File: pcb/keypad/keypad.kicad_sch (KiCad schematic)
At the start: 0 parts

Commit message: Keypad Layout Done V1
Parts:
- added BT1: Battery_Cell, Connector_JST:JST_PH_S2B-PH-SM4-TB_1x02-1MP_P2.00mm_Horizontal, symbol Device:Battery_Cell
- added J1: Conn_01x24_Male, Connector_FFC-FPC:TE_2-1734839-4_1x24-1MP_P0.5mm_Horizontal, symbol Connector:Conn_01x24_Male
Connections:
- net Keys/KC0: now also J1.16 (Pin_16)
- net Keys/KC1: now also J1.15 (Pin_15)
- net Keys/KC2: now also J1.14 (Pin_14)
- net Keys/KC3: now also J1.13 (Pin_13)
- net Keys/KC4: now also J1.12 (Pin_12)
- net Keys/KC5: now also J1.11 (Pin_11)
- net Keys/KC6: now also J1.10 (Pin_10)
- net Keys/KR0: now also J1.23 (Pin_23)
- net Keys/KR1: now also J1.22 (Pin_22)
- net Keys/KR2: now also J1.21 (Pin_21)
- net Keys/KR3: now also J1.20 (Pin_20)
- net Keys/KR4: now also J1.19 (Pin_19)
- net Keys/KR5: now also J1.18 (Pin_18)
- net Keys/KR6: now also J1.17 (Pin_17)
- net Keys/ON: now also J1.9 (Pin_9)
- new net GND: BT1.2 (-), J1.24 (Pin_24), J1.6 (Pin_6), J1.7 (Pin_7), J1.8 (Pin_8)
- new net VBAT: BT1.1 (+), J1.2 (Pin_2), J1.3 (Pin_3), J1.4 (Pin_4), J1.5 (Pin_5)
- no-connect marks 0 -> 1

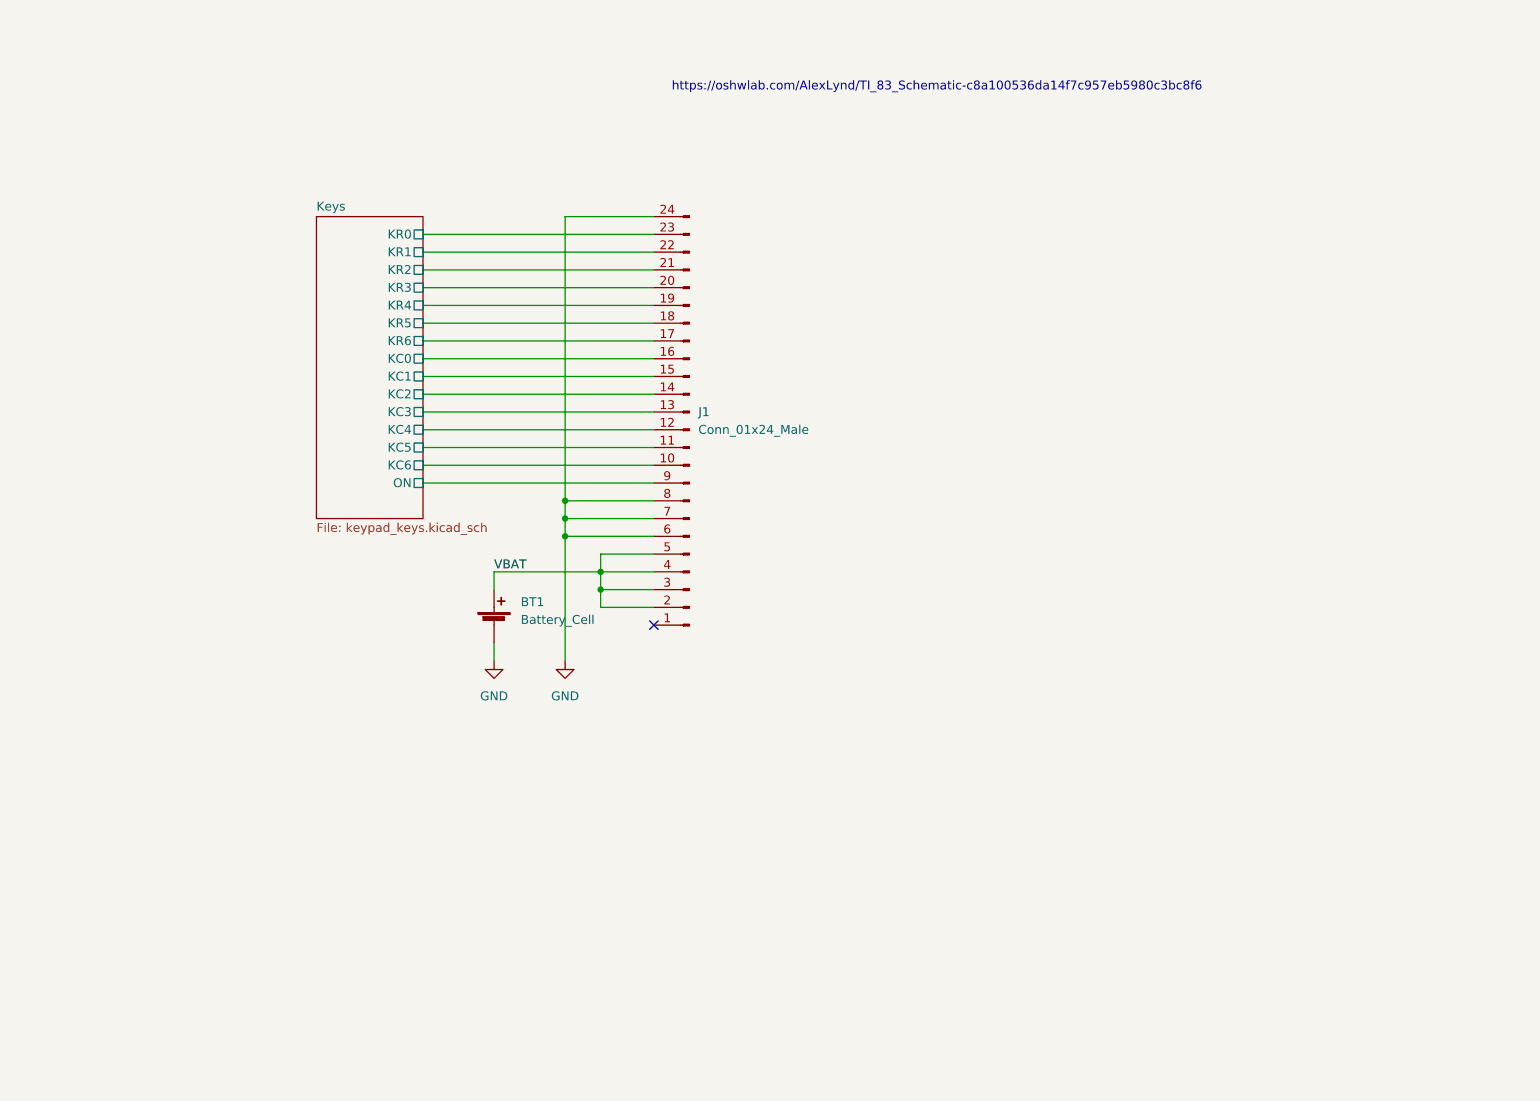
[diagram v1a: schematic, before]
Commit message: Keypad Schematic Update - Comm Interface
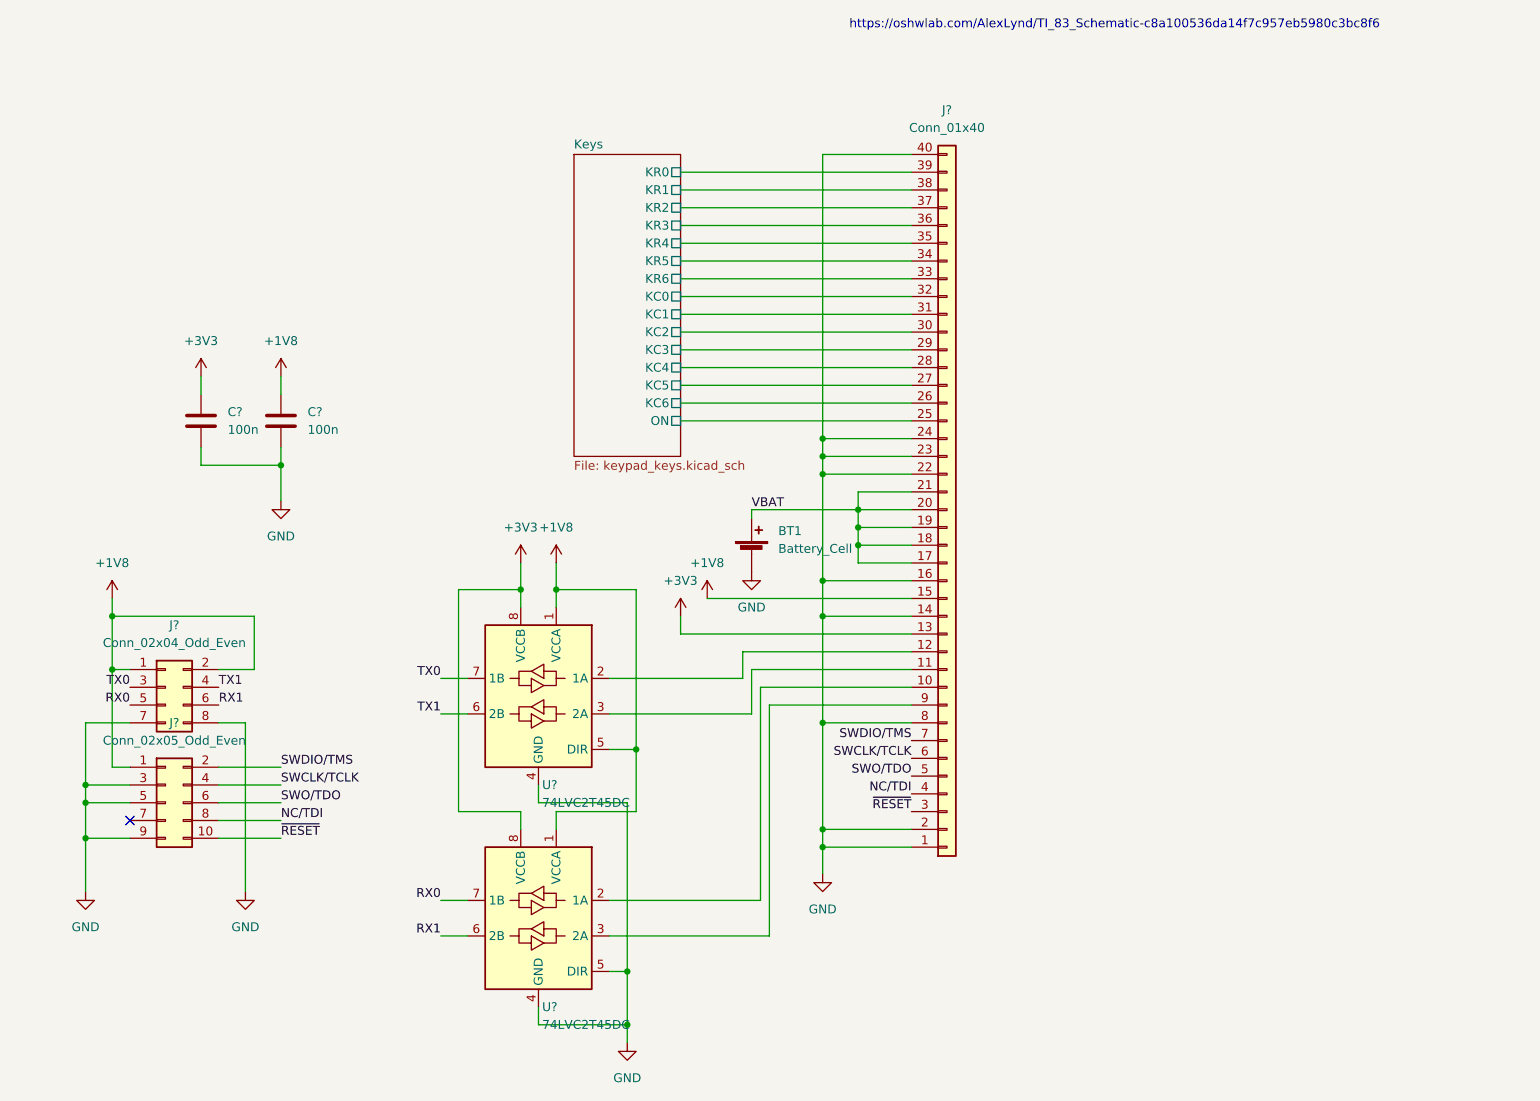
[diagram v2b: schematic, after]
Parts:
- removed J1: Conn_01x24_Male, Connector_FFC-FPC:TE_2-1734839-4_1x24-1MP_P0.5mm_Horizontal, symbol Connector:Conn_01x24_Male
- added C? (x2): 100n, Capacitor_SMD:C_0805_2012Metric, symbol Device:C
- added J?: Conn_01x40, Connector_FFC-FPC:TE_4-1734839-0_1x40-1MP_P0.5mm_Horizontal, symbol Connector_Generic:Conn_01x40
- added J?: Conn_02x04_Odd_Even, Connector_PinHeader_1.27mm:PinHeader_2x04_P1.27mm_Vertical_SMD, symbol Connector_Generic:Conn_02x04_Odd_Even
- added J?: Conn_02x05_Odd_Even, Connector_PinHeader_1.27mm:PinHeader_2x05_P1.27mm_Vertical_SMD, symbol Connector_Generic:Conn_02x05_Odd_Even
- added U? (x2): 74LVC2T45DC, Package_SO:VSSOP-8_2.3x2mm_P0.5mm, symbol Logic_LevelTranslator:74LVC2T45DC
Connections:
- net GND: now also C?.2, C?.2, J?.1 (Pin_1), J?.14 (Pin_14), J?.16 (Pin_16), J?.2 (Pin_2), J?.22 (Pin_22), J?.23 (Pin_23), J?.24 (Pin_24), J?.3 (Pin_3), J?.40 (Pin_40), J?.5 (Pin_5), J?.7 (Pin_7), J?.8 (Pin_8), J?.8 (Pin_8), J?.9 (Pin_9), U?.4 (GND), U?.4 (GND), U?.5 (DIR)
- net Keys/KC0: now also J?.32 (Pin_32)
- net Keys/KC1: now also J?.31 (Pin_31)
- net Keys/KC2: now also J?.30 (Pin_30)
- net Keys/KC3: now also J?.29 (Pin_29)
- net Keys/KC4: now also J?.28 (Pin_28)
- net Keys/KC5: now also J?.27 (Pin_27)
- net Keys/KC6: now also J?.26 (Pin_26)
- net Keys/KR0: now also J?.39 (Pin_39)
- net Keys/KR1: now also J?.38 (Pin_38)
- net Keys/KR2: now also J?.37 (Pin_37)
- net Keys/KR3: now also J?.36 (Pin_36)
- net Keys/KR4: now also J?.35 (Pin_35)
- net Keys/KR5: now also J?.34 (Pin_34)
- net Keys/KR6: now also J?.33 (Pin_33)
- net Keys/ON: now also J?.25 (Pin_25)
- net VBAT: now also J?.17 (Pin_17), J?.18 (Pin_18), J?.19 (Pin_19), J?.20 (Pin_20), J?.21 (Pin_21)
- new net: J?.10 (Pin_10), U?.2 (1A)
- new net: J?.11 (Pin_11), U?.3 (2A)
- new net: J?.12 (Pin_12), U?.2 (1A)
- new net: J?.9 (Pin_9), U?.3 (2A)
- new net +1V8: C?.1, J?.1 (Pin_1), J?.1 (Pin_1), J?.15 (Pin_15), J?.2 (Pin_2), U?.1 (VCCA), U?.1 (VCCA), U?.5 (DIR)
- new net +3V3: C?.1, J?.13 (Pin_13), U?.8 (VCCB), U?.8 (VCCB)
- new net NC/TDI: J?.4 (Pin_4), J?.8 (Pin_8)
- new net RX0: J?.5 (Pin_5), U?.7 (1B)
- new net RX1: J?.6 (Pin_6), U?.6 (2B)
- new net SWCLK/TCLK: J?.4 (Pin_4), J?.6 (Pin_6)
- new net SWDIO/TMS: J?.2 (Pin_2), J?.7 (Pin_7)
- new net SWO/TDO: J?.5 (Pin_5), J?.6 (Pin_6)
- new net TX0: J?.3 (Pin_3), U?.7 (1B)
- new net TX1: J?.4 (Pin_4), U?.6 (2B)
- new net ~{RESET}: J?.10 (Pin_10), J?.3 (Pin_3)
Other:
- moved on the sheet: BT1

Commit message: Keypad Layout Update - JTAG/UART
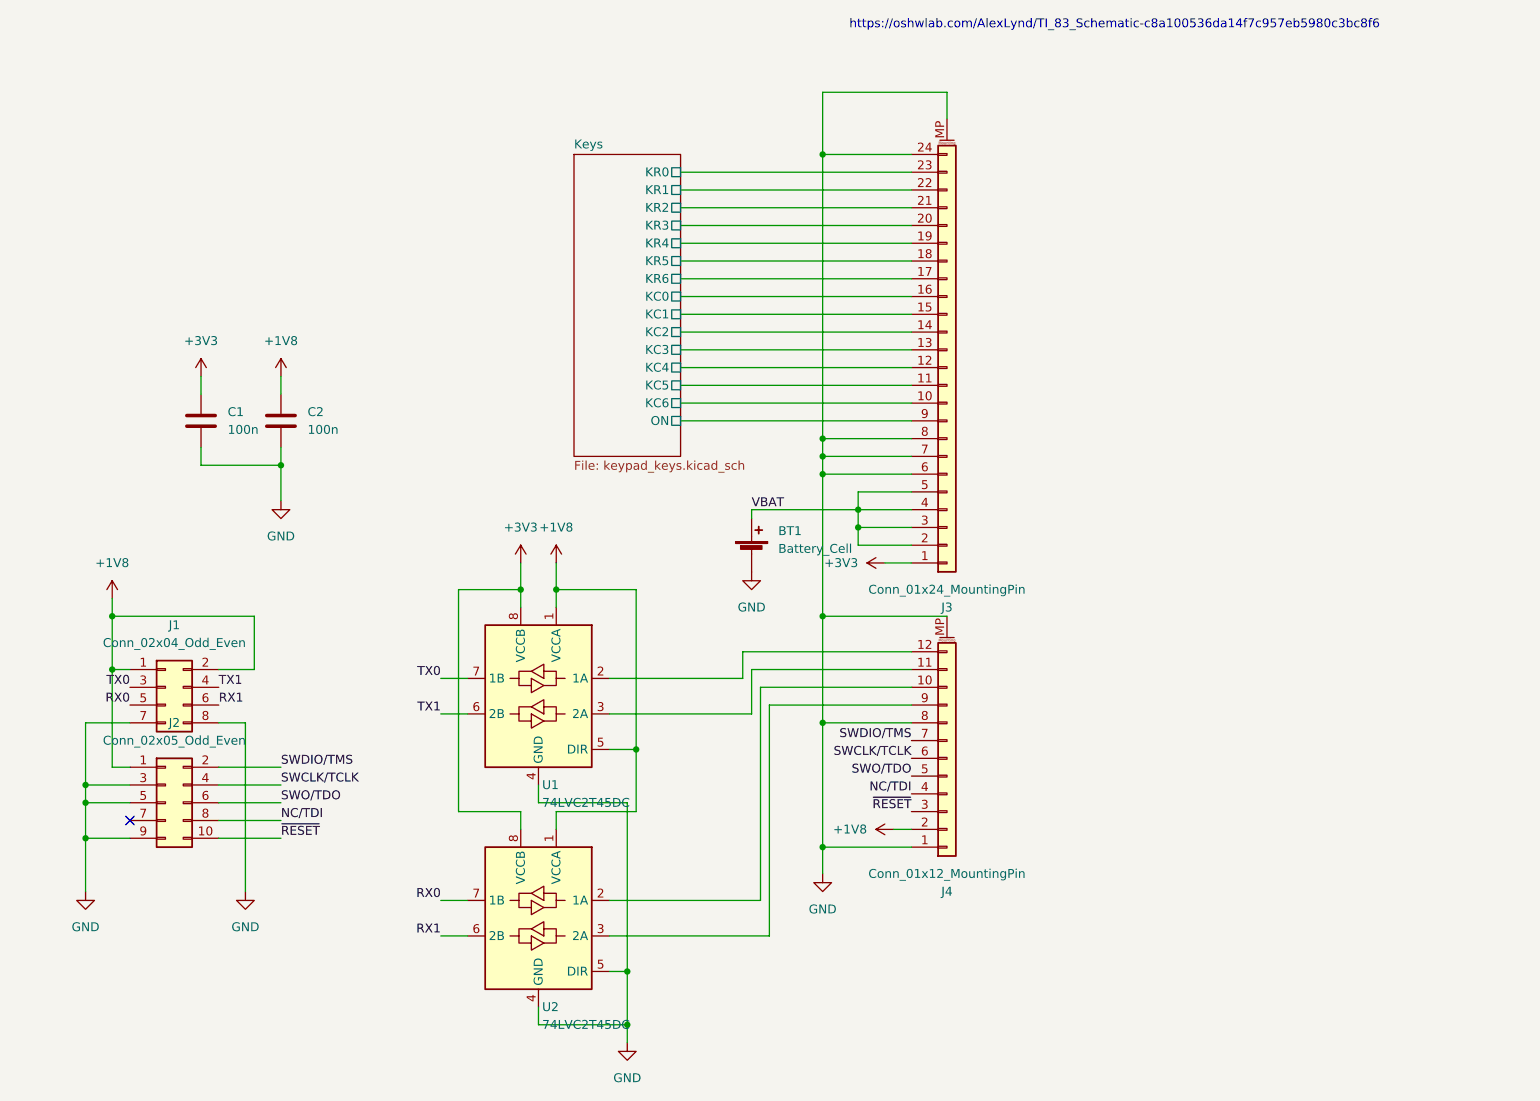
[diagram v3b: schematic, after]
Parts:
- removed J?: Conn_01x40, Connector_FFC-FPC:TE_4-1734839-0_1x40-1MP_P0.5mm_Horizontal, symbol Connector_Generic:Conn_01x40
- added J3: Conn_01x24_MountingPin, Connector_FFC-FPC:TE_2-1734839-4_1x24-1MP_P0.5mm_Horizontal, symbol Connector_Generic_MountingPin:Conn_01x24_MountingPin
- added J4: Conn_01x12_MountingPin, Connector_FFC-FPC:TE_1-1734839-2_1x12-1MP_P0.5mm_Horizontal, symbol Connector_Generic_MountingPin:Conn_01x12_MountingPin
- gave numbers to parts that had none: 6
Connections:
- net +1V8: now also J4.2 (Pin_2)
- net +3V3: now also J3.1 (Pin_1)
- net GND: now also J3.24 (Pin_24), J3.6 (Pin_6), J3.7 (Pin_7), J3.8 (Pin_8), J3.MP (MountPin), J4.1 (Pin_1), J4.8 (Pin_8), J4.MP (MountPin)
- net Keys/KC0: now also J3.16 (Pin_16)
- net Keys/KC1: now also J3.15 (Pin_15)
- net Keys/KC2: now also J3.14 (Pin_14)
- net Keys/KC3: now also J3.13 (Pin_13)
- net Keys/KC4: now also J3.12 (Pin_12)
- net Keys/KC5: now also J3.11 (Pin_11)
- net Keys/KC6: now also J3.10 (Pin_10)
- net Keys/KR0: now also J3.23 (Pin_23)
- net Keys/KR1: now also J3.22 (Pin_22)
- net Keys/KR2: now also J3.21 (Pin_21)
- net Keys/KR3: now also J3.20 (Pin_20)
- net Keys/KR4: now also J3.19 (Pin_19)
- net Keys/KR5: now also J3.18 (Pin_18)
- net Keys/KR6: now also J3.17 (Pin_17)
- net Keys/ON: now also J3.9 (Pin_9)
- net NC/TDI: now also J4.4 (Pin_4)
- net SWCLK/TCLK: now also J4.6 (Pin_6)
- net SWDIO/TMS: now also J4.7 (Pin_7)
- net SWO/TDO: now also J4.5 (Pin_5)
- net VBAT: now also J3.2 (Pin_2), J3.3 (Pin_3), J3.4 (Pin_4), J3.5 (Pin_5)
- net ~{RESET}: now also J4.3 (Pin_3)
- net at U2.2 (1A): now also J4.10 (Pin_10)
- net at U1.3 (2A): now also J4.11 (Pin_11)
- net at U1.2 (1A): now also J4.12 (Pin_12)
- net at U2.3 (2A): now also J4.9 (Pin_9)

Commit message: Keypad bugfix, pulling in submodules
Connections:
- net GND: no longer J3.8 (Pin_8)
- new net Keys/KR7: J3.8 (Pin_8)
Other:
- sheet Keys ports: added KR7; removed none
